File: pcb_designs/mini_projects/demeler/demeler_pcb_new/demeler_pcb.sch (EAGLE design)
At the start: 36 parts, among them IC1 ATMEGA328, IC2 L293D, J2 1445055-5, Q1 16MHZ, X1 RJ45-6X, X2 KUSBVX

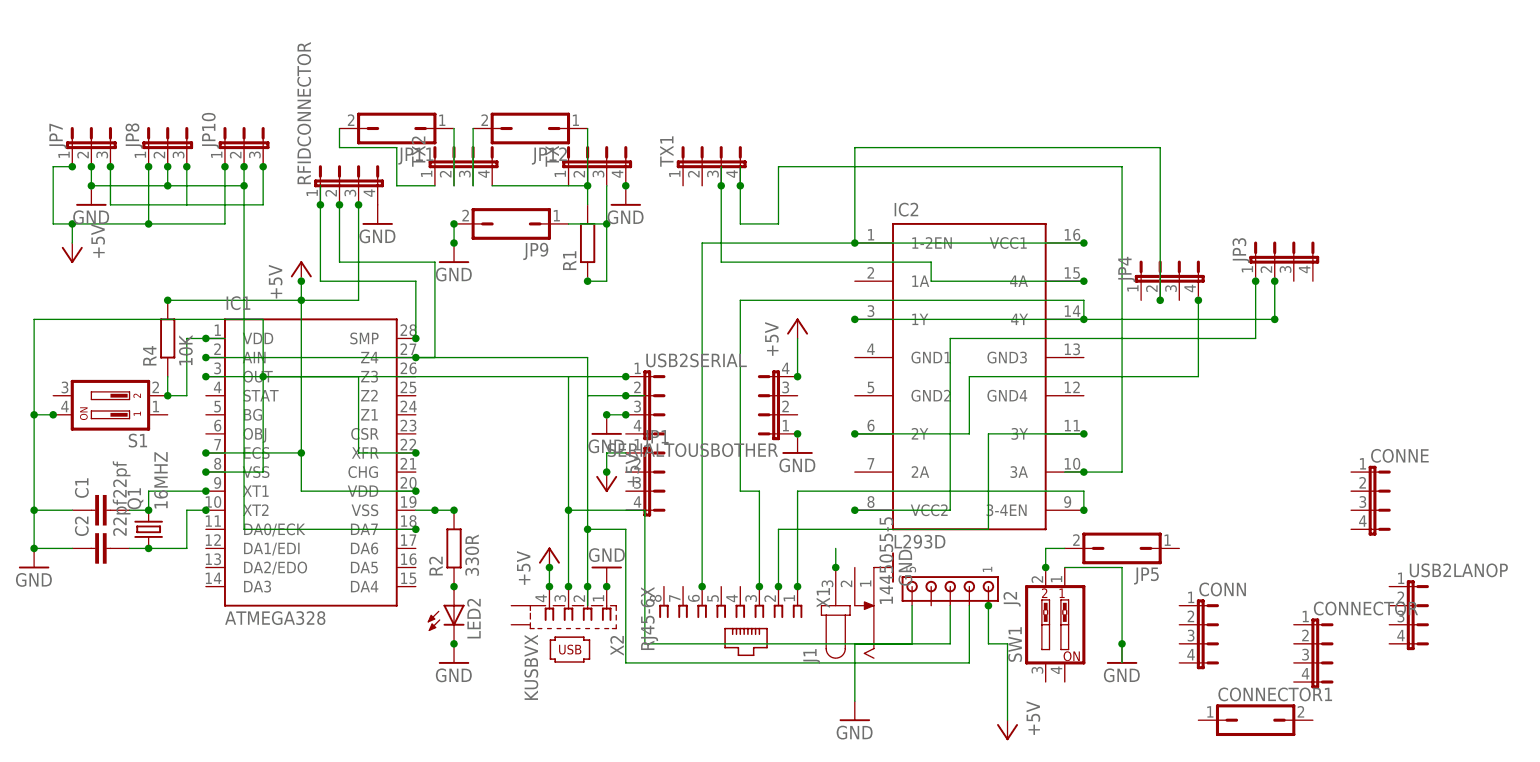
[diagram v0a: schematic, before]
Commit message: 
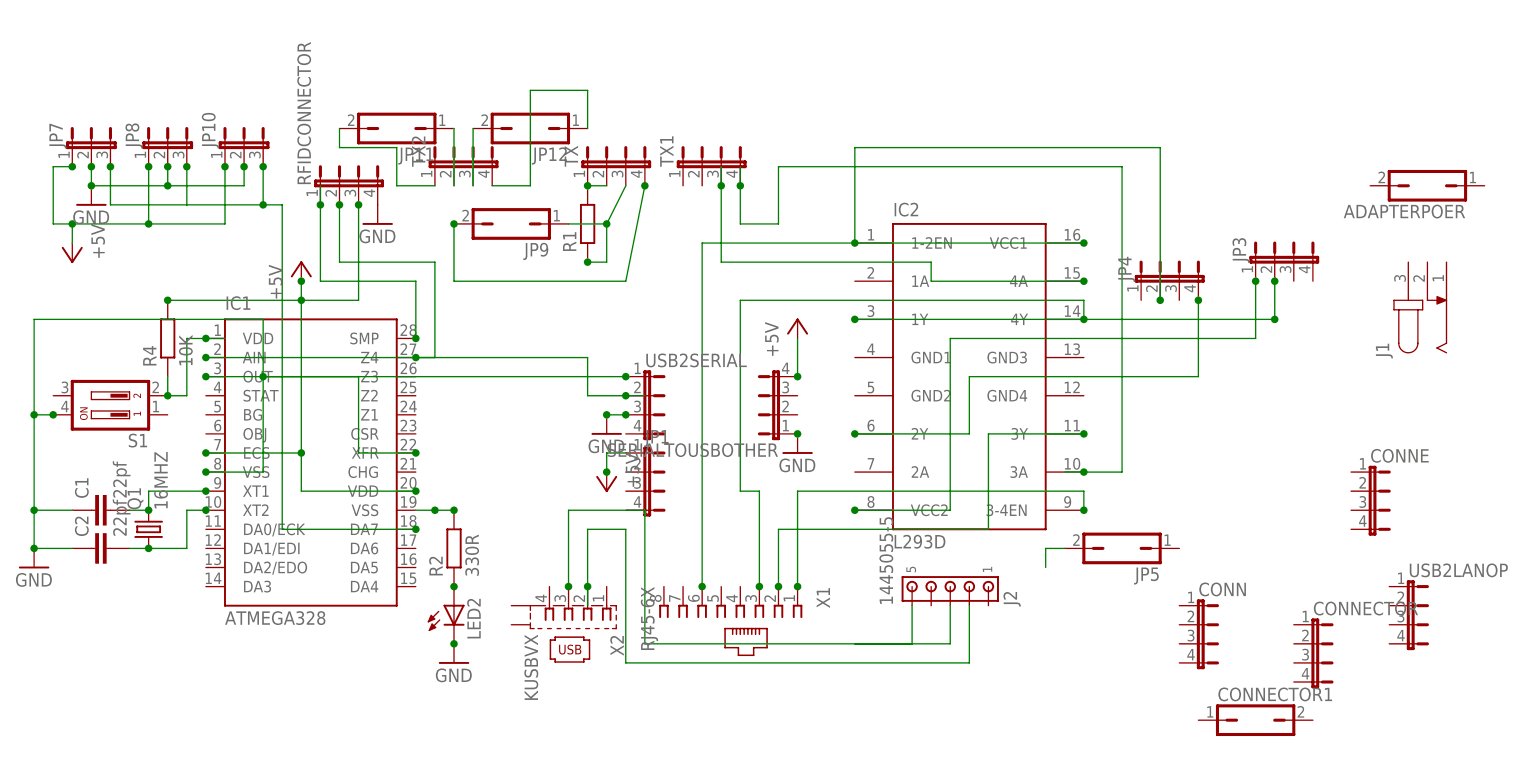
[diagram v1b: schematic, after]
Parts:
- removed SW1: (no value), special:SW_DIP-2
- added ADAPTERPOER: (no value), jumper:JP1Q
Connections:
- new net N$16: IC1.AIN, USB2SERIAL.2
- new net N$19: J2.5
- new net N$21: JP9.2, TX.4
- net +5V: no longer J2.1, X2.4
- net GND: no longer IC1.DA7, J1.1, J2.5, JP9.2, SW1.1, TX.4, X2.1
- net N$17: now also TX.1
- net N$20: no longer IC1.AIN, USB2SERIAL.2
- net N$23: no longer SW1.2
- net N$26: now also IC1.DA7
- net N$3: now also IC1.OUT, USB2SERIAL.1; no longer J1.3
- net N$4: no longer IC1.OUT, USB2SERIAL.1
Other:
- moved on the sheet: J1, R1, TX
